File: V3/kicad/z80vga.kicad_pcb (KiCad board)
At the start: 2 copper layers, 135 x 100 mm, 55 parts, among them J2002 Conn_02x08_Odd_Even, J2120 USB_B, J2122 Conn_01x02_Male, J2230 Micro_SD_Card_Det, SW2110 SW_Push, U2000 Z8-L180-S180-180-PQFP-80, U2001 GAL16V8, U2002 74HCT273, U2003 14.7456 MHz, U2110 LM555xM, U2120 MCP2221AxP, U2230 74LS07, U2231 LP2985-3.3, U3000 SST39SF040, U3001 AS6C4008-55PCN

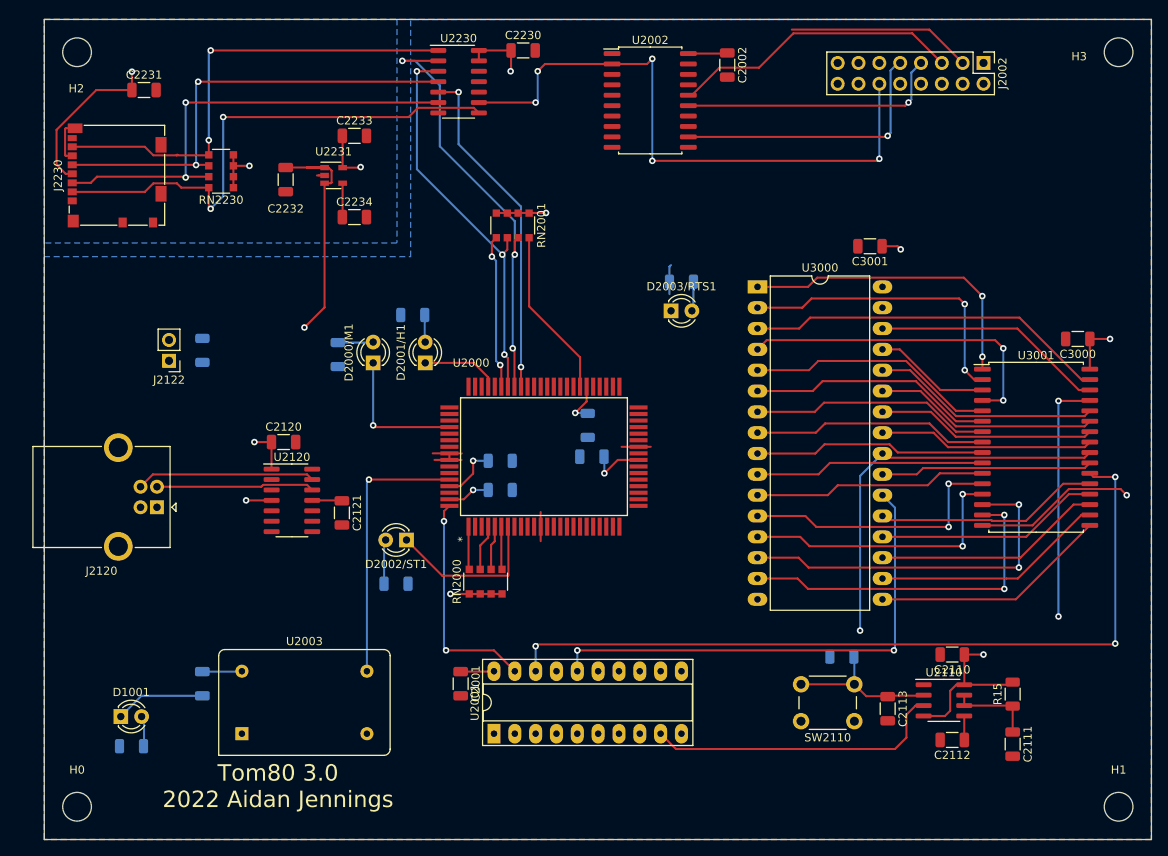
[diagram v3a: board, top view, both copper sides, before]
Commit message: routed last of non-bus lines
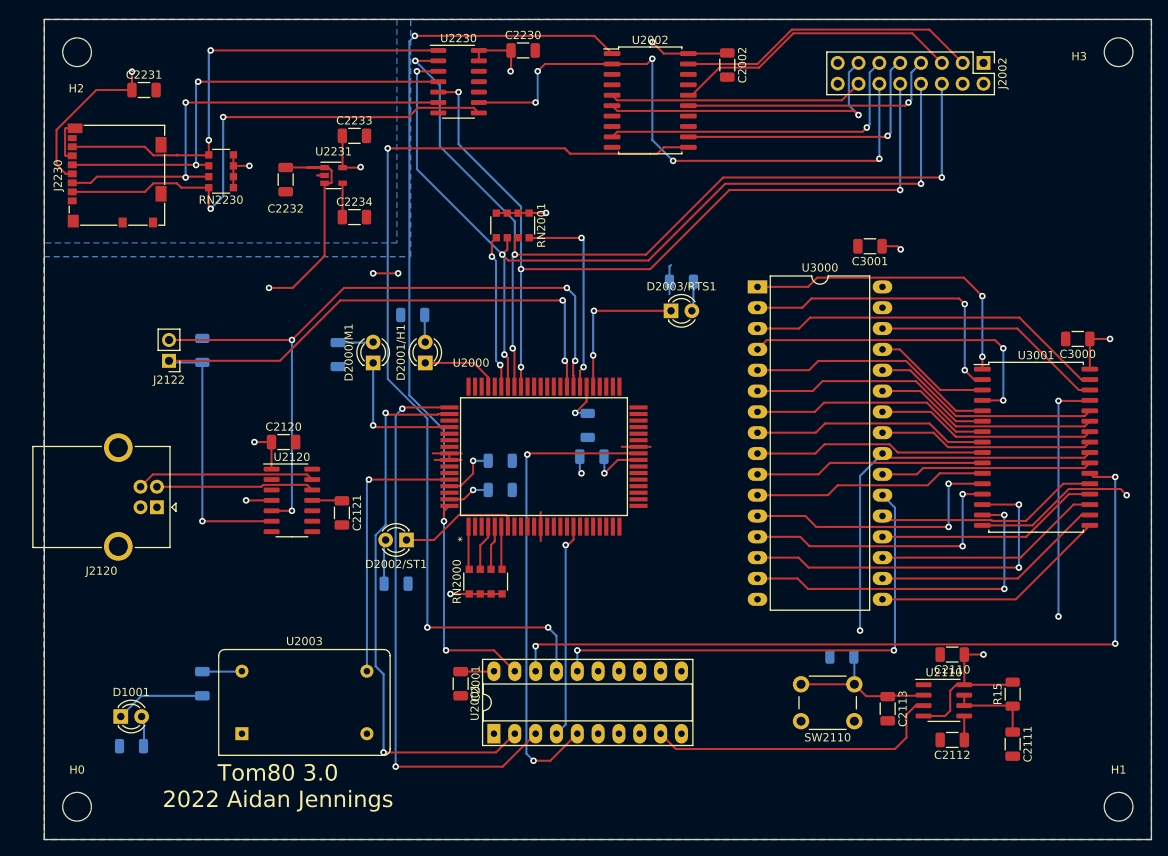
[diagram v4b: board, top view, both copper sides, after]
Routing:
- net Net-(U2001-Pad17): track 0.00 -> 118.2 mm, vias 0 -> 3
- net /2000_CPU/RX: track 0.00 -> 93.7 mm, vias 0 -> 3
- net /2000_CPU/TX: track 0.00 -> 87.0 mm, vias 0 -> 4
- net /2000_CPU/C_RST: track 27.4 -> 113.6 mm, vias 2 -> 3
- net /2000_CPU/IORQ: track 0.00 -> 68.5 mm, vias 0 -> 2
- net /2000_CPU/CKS: track 48.0 -> 115.4 mm, vias 3 -> 4
- net /2000_CPU/MREQ: track 0.00 -> 67.2 mm, vias 0 -> 2
- net /2000_CPU/RXS: track 53.1 -> 117.4 mm, vias 3 -> 4
- net /2000_CPU/TXS: track 41.5 -> 104.7 mm, vias 2 -> 4
- net /2000_CPU/A19: track 0.00 -> 58.4 mm, vias 0 -> 2
- net /2000_CPU/CS3: track 0.00 -> 40.0 mm, vias 0 -> 1
- net /2000_CPU/CS2: track 0.00 -> 37.8 mm, vias 0 -> 1
- net /2000_CPU/CS1: track 0.00 -> 31.1 mm
- net /2000_CPU/A7: track 30.4 -> 56.7 mm, vias 0 -> 1
- net /2000_CPU/RTS0: track 0.00 -> 18.7 mm, vias 0 -> 2
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
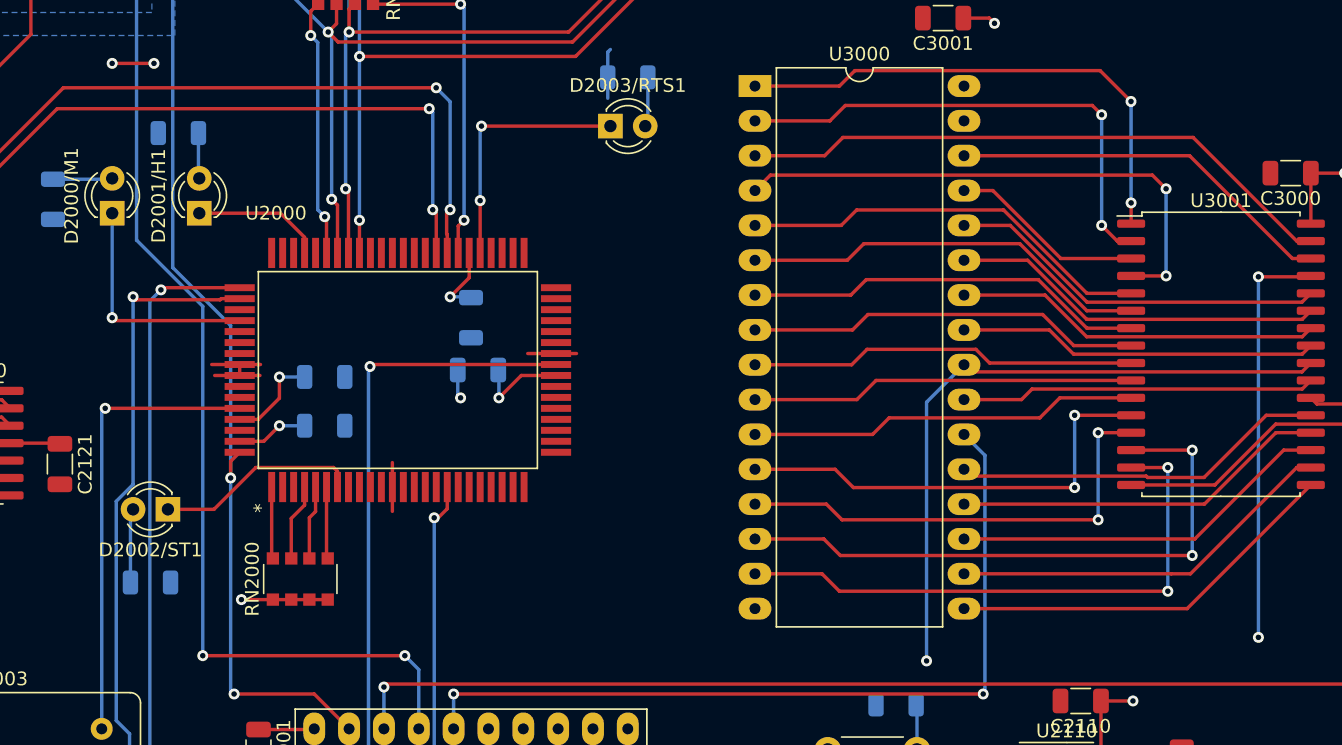
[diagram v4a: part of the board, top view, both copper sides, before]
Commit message: attempted to route memory lines
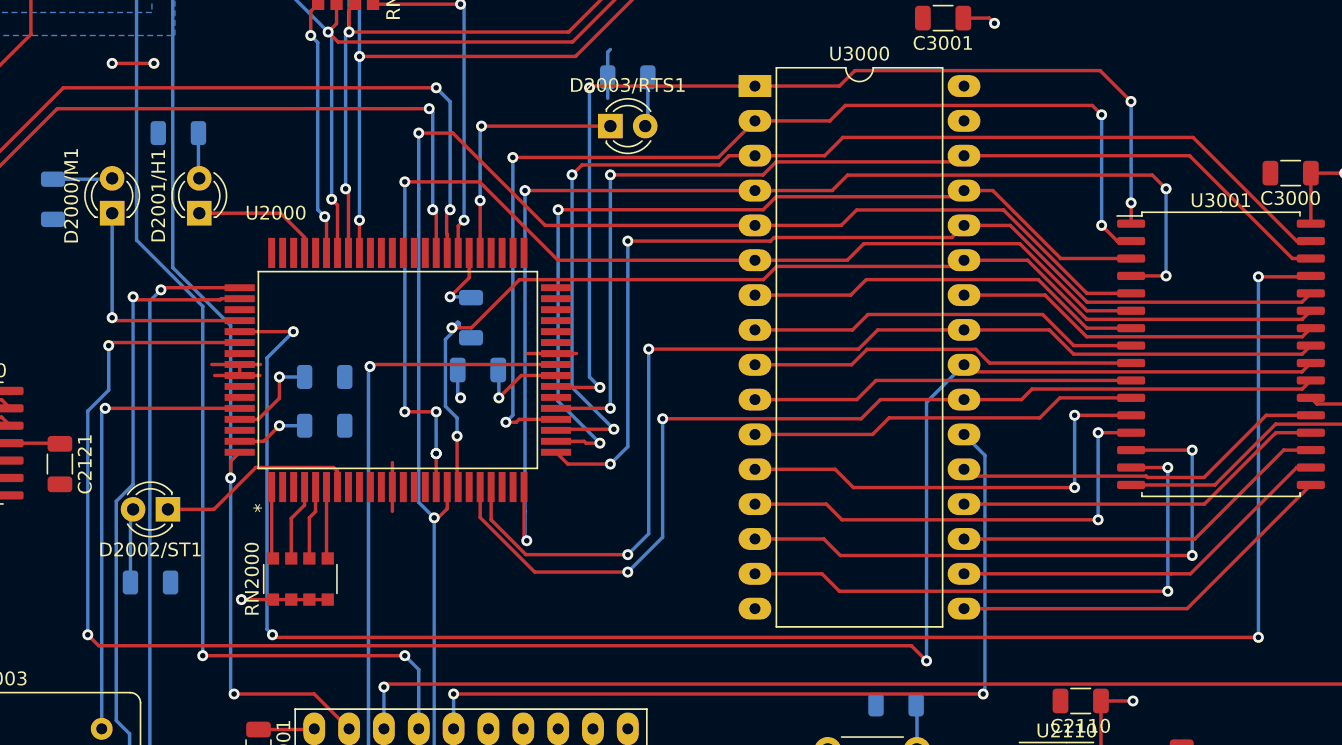
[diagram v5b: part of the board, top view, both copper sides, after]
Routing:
- net /2000_CPU/WR: track 30.1 -> 129.1 mm, vias 2 -> 4
- net /2000_CPU/RD: track 48.5 -> 141.8 mm, vias 1 -> 3
- net /2000_CPU/A7: track 56.7 -> 112.5 mm, vias 1 -> 2
- net /2000_CPU/A8: track 27.3 -> 80.2 mm, vias 0 -> 2
- net /2000_CPU/A11: track 26.3 -> 78.9 mm, vias 0 -> 2
- net /2000_CPU/A6: track 29.9 -> 82.4 mm, vias 0 -> 5
- net /2000_CPU/A14: track 14.2 -> 65.9 mm, vias 0 -> 2
- net /2000_CPU/A10: track 25.9 -> 75.3 mm, vias 0 -> 2
- net /2000_CPU/A17: track 28.4 -> 75.7 mm, vias 0 -> 2
- net /2000_CPU/A12: track 39.8 -> 86.1 mm, vias 2 -> 4
- net /2000_CPU/A13: track 27.9 -> 74.0 mm, vias 0 -> 2
- net /2000_CPU/A16: track 36.7 -> 78.7 mm, vias 2 -> 4
- net /2000_CPU/A15: track 44.2 -> 82.2 mm, vias 0 -> 2
- net /2000_CPU/A18: track 37.7 -> 75.2 mm, vias 2 -> 4

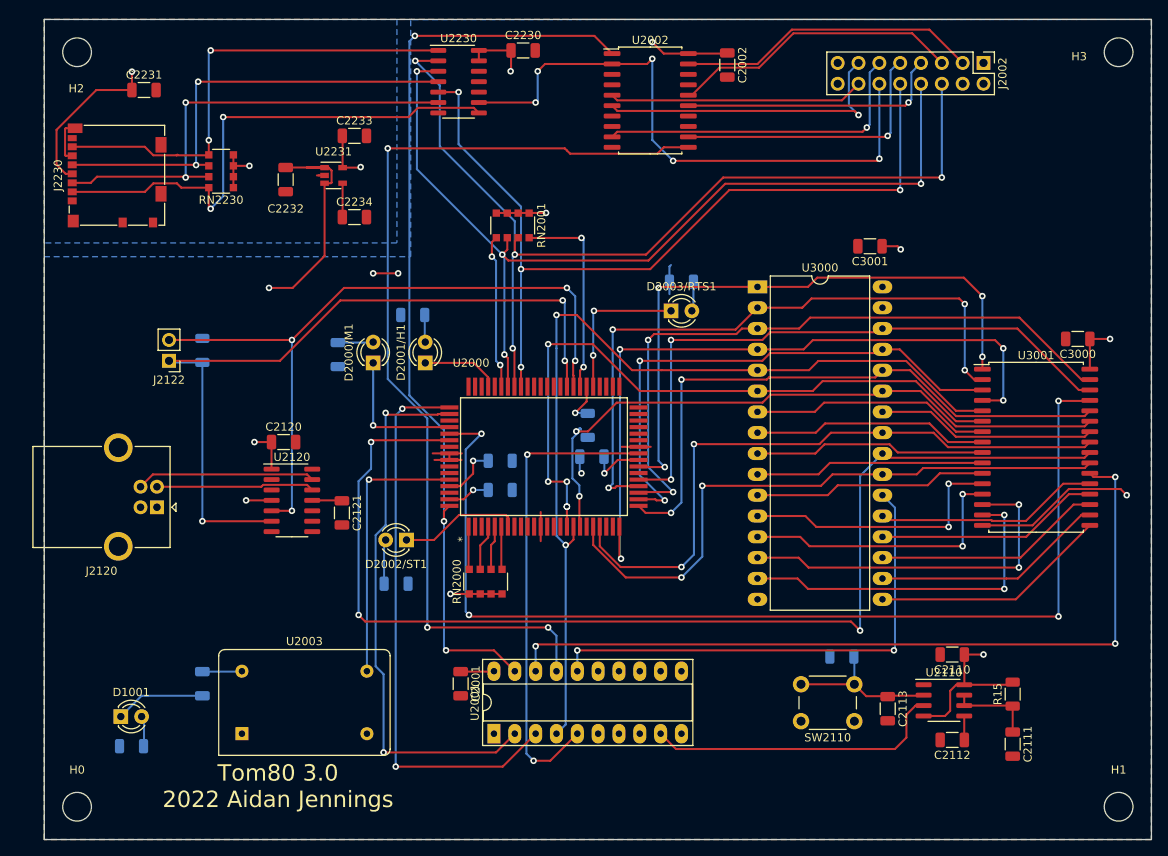
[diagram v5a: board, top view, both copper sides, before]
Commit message: Added new symbol and footprint
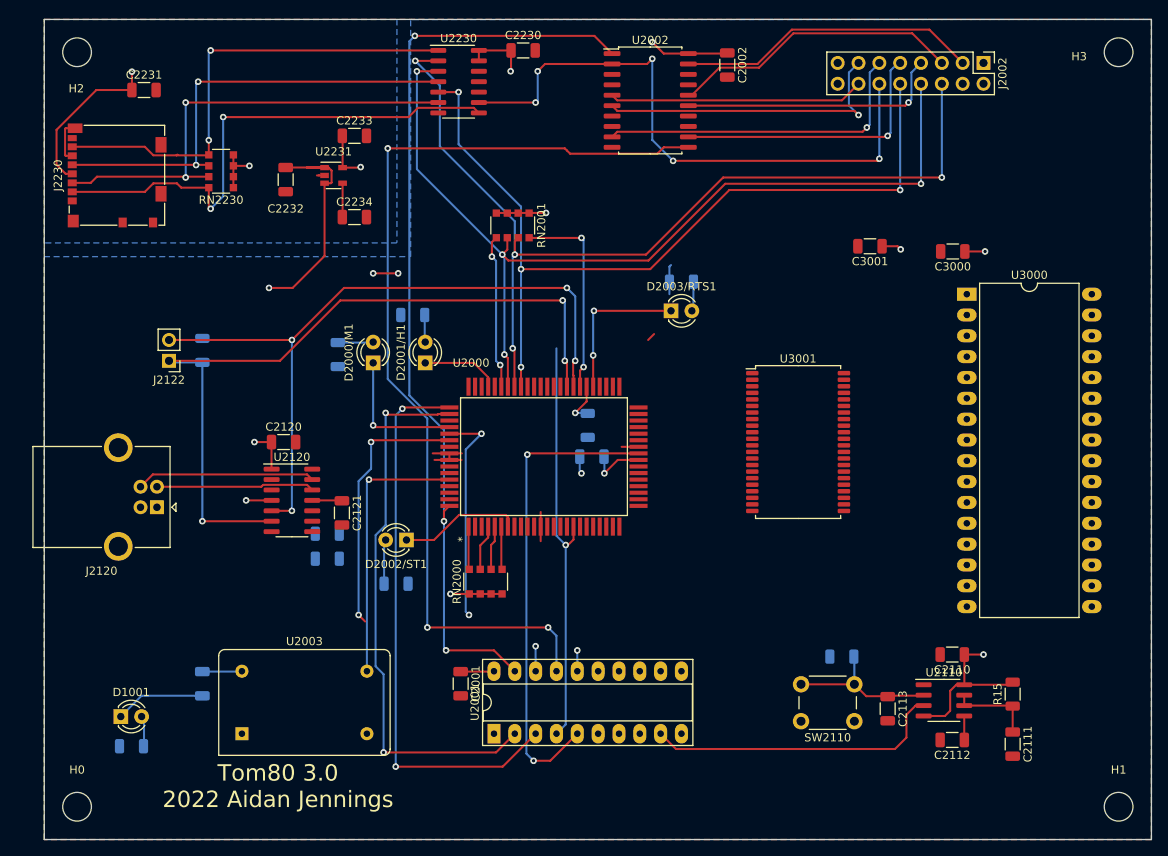
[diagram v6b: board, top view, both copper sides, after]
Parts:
- U3001: value AS6C4008-55PCN -> AS6C8008-55_TSOP; footprint Package_SO:SSOP-32_11.305x20.495mm_P1.27mm -> Package_SO:TSOP-II-44_10.16x18.41mm_P0.8mm
- moved U3001 29.0 mm to (121.9, 81.5)
- moved U3000 25.5 mm to (142.5, 63.5)
- moved R2004 22.9 mm to (64.5, 92.7), turned to 0 degrees
- moved R2005 22.7 mm to (64.5, 95.8), turned to 0 degrees
- moved C3000 18.6 mm to (140.8, 58.3)
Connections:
- U3001 pad 1: /2000_CPU/A18 -> /2000_CPU/A4
- U3001 pad 10: /2000_CPU/A2 -> /2000_CPU/D1
- U3001 pad 11: /2000_CPU/A1 -> +5V
- U3001 pad 12: /2000_CPU/A0 -> GND
- U3001 pad 13: /2000_CPU/D0 -> /2000_CPU/D2
- U3001 pad 14: /2000_CPU/D1 -> /2000_CPU/D3
- U3001 pad 15: /2000_CPU/D2 -> Net-(U3001-Pad15)
- U3001 pad 16: GND -> Net-(U3001-Pad16)
- U3001 pad 17: /2000_CPU/D3 -> /2000_CPU/WR
- U3001 pad 18: /2000_CPU/D4 -> /2000_CPU/A19
- U3001 pad 19: /2000_CPU/D5 -> /2000_CPU/A18
- U3001 pad 2: /2000_CPU/A16 -> /2000_CPU/A3
- U3001 pad 20: /2000_CPU/D6 -> /2000_CPU/A17
- U3001 pad 21: /2000_CPU/D7 -> /2000_CPU/A16
- U3001 pad 22: /2000_CPU/RAM_CS -> /2000_CPU/A15
- U3001 pad 23: /2000_CPU/A10 -> /2000_CPU/A14
- U3001 pad 24: /2000_CPU/RD -> /2000_CPU/A13
- U3001 pad 25: /2000_CPU/A11 -> /2000_CPU/A12
- U3001 pad 26: /2000_CPU/A9 -> /2000_CPU/A11
- U3001 pad 27: /2000_CPU/A8 -> /2000_CPU/A10
- U3001 pad 28: /2000_CPU/A13 -> /2000_CPU/A9
- U3001 pad 29: /2000_CPU/WR -> Net-(U3001-Pad29)
- U3001 pad 3: /2000_CPU/A14 -> /2000_CPU/A2
- U3001 pad 30: /2000_CPU/A17 -> Net-(U3001-Pad30)
- U3001 pad 31: /2000_CPU/A15 -> /2000_CPU/D4
- U3001 pad 32: +5V -> /2000_CPU/D5
- U3001 pad 4: /2000_CPU/A12 -> /2000_CPU/A1
- U3001 pad 5: /2000_CPU/A7 -> /2000_CPU/A0
- U3001 pad 6: /2000_CPU/A6 -> /2000_CPU/RAM_CS
- U3001 pad 7: /2000_CPU/A5 -> Net-(U3001-Pad7)
- U3001 pad 8: /2000_CPU/A4 -> Net-(U3001-Pad8)
- U3001 pad 9: /2000_CPU/A3 -> /2000_CPU/D0
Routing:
- net /2000_CPU/RD: track 141.8 -> 32.5 mm, vias 3 -> 2
- net /2000_CPU/WR: track 129.1 -> 27.2 mm, vias 4 -> 2
- net /2000_CPU/RAM_CS: track 97.5 -> 3.05 mm, vias 3 -> 1
- net /2000_CPU/A12: track 86.1 -> 0.00 mm, vias 4 -> 0
- net /2000_CPU/A6: track 82.4 -> 0.01 mm, vias 5 -> 0
- net /2000_CPU/A15: track 82.2 -> 1.03 mm, vias 2 -> 0
- net /2000_CPU/A8: track 80.2 -> 0.12 mm, vias 2 -> 0
- net /2000_CPU/A11: track 78.9 -> 0.00 mm, vias 2 -> 0
- net /2000_CPU/A16: track 78.7 -> 0.00 mm, vias 4 -> 0
- net /2000_CPU/A17: track 75.7 -> 0.00 mm, vias 2 -> 0
- net /2000_CPU/A10: track 75.3 -> 0.00 mm, vias 2 -> 0
- net /2000_CPU/A18: track 75.2 -> 0.00 mm, vias 4 -> 0
- net /2000_CPU/A13: track 74.0 -> 0.00 mm, vias 2 -> 0
- net /2000_CPU/A14: track 65.9 -> 0.00 mm, vias 2 -> 0
- net /2000_CPU/A7: track 112.5 -> 50.7 mm, vias 2 -> 1
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
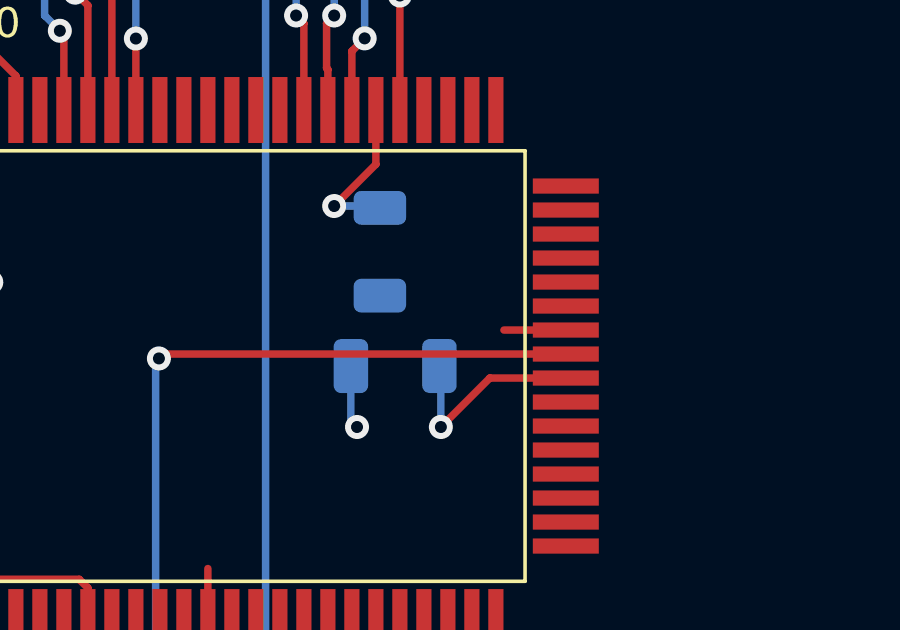
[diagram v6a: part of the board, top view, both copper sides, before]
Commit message: CTS0 no longer drives an LED
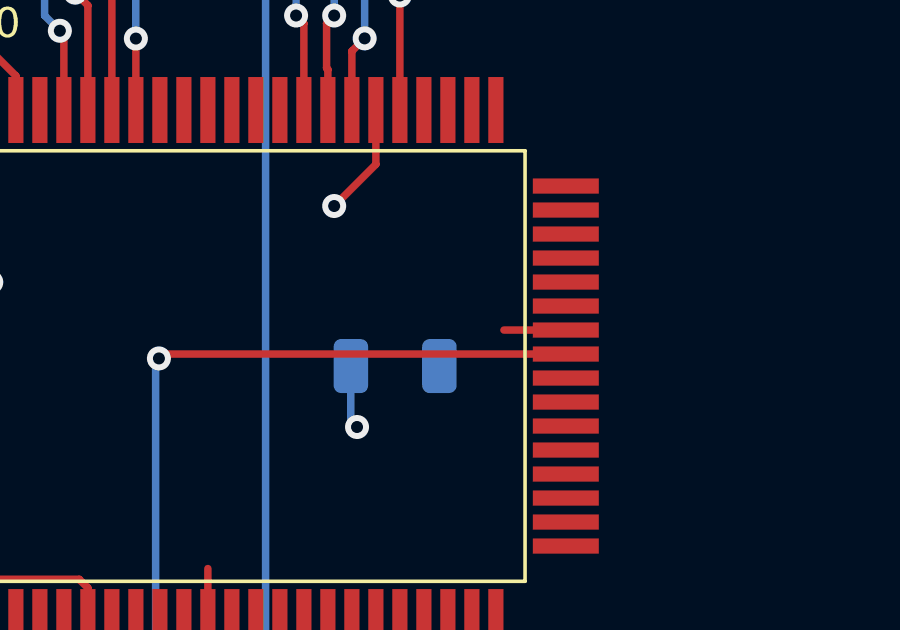
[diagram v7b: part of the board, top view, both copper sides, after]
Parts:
- removed R2006: R, Resistor_SMD:R_1206_3216Metric
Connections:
- U2001 pad 6: Net-(U2001-Pad6) -> /2000_CPU/CTS0
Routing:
- net +5V: track 113.4 -> 107.0 mm, vias 13 -> 12
- net /2000_CPU/CTS0: track 5.33 -> 3.78 mm

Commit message: Final cleanup before memory routing
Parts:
- moved C2000 16.6 mm to (102.6, 67.8), turned to 90 degrees
- moved R2004 3.41 mm to (63.0, 95.8)
- moved R2005 3.41 mm to (63.0, 98.8)
- moved U3000 2.03 mm to (140.5, 63.5)
- moved U3001 2.03 mm to (121.9, 83.6)
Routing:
- net /2000_CPU/ROM_CS: track 2.54 -> 97.3 mm, vias 1 -> 3
- net /2000_CPU/CTS0: track 3.78 -> 75.3 mm, vias 1 -> 2
- net /2000_CPU/RD: track 32.5 -> 0.00 mm, vias 2 -> 0
- net /2000_CPU/WR: track 27.2 -> 0.01 mm, vias 2 -> 0
- net /2000_CPU/A7: track 50.7 -> 26.3 mm
- net /2000_CPU/BUSREQ: track 0.00 -> 20.3 mm, vias 0 -> 1
- net /2000_CPU/WAIT: track 0.00 -> 18.6 mm, vias 0 -> 1
- net GND: track 32.7 -> 50.9 mm, vias 1 -> 0
- net +5V: track 107.0 -> 109.6 mm, vias 12 -> 13
- net /2000_CPU/A15: track 1.03 -> 0.00 mm
